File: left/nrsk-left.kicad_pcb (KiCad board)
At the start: 2 copper layers, 172.6 x 132.6 mm, 139 parts, among them J1 PJ-320D, J2 USB-C, J3 OLED 128x32, SW1 Esc, SW10 1, SW11 2, SW12 3, SW13 4, SW14 5, SW15 6, SW16 16, SW17 Tab, SW18 Q, SW19 W, SW2 F1, SW20 E, SW21 R, SW22 T, SW23 23, SW24 Ctrl, SW25 A, SW26 S, SW27 D, SW28 F, SW29 G, SW3 F2, SW30 30, SW31 Shift, SW32 Z, SW33 X, SW34 C, SW35 V, SW36 B, SW37 37, SW38 Ctrl, SW39 Opt, SW4 F3, SW40 Cmd, SW41 Space, SW42 Space, SW43 Space, SW44 44, SW5 F4, SW6 F5, SW7 F6, SW8 8, SW9 `, U1 RP2040, U2 USBLC6-2SC6, U3 AS5600-ASOM, U4 AP2112K-3.3, U5 W25Q128JVS, Y1 12MHz

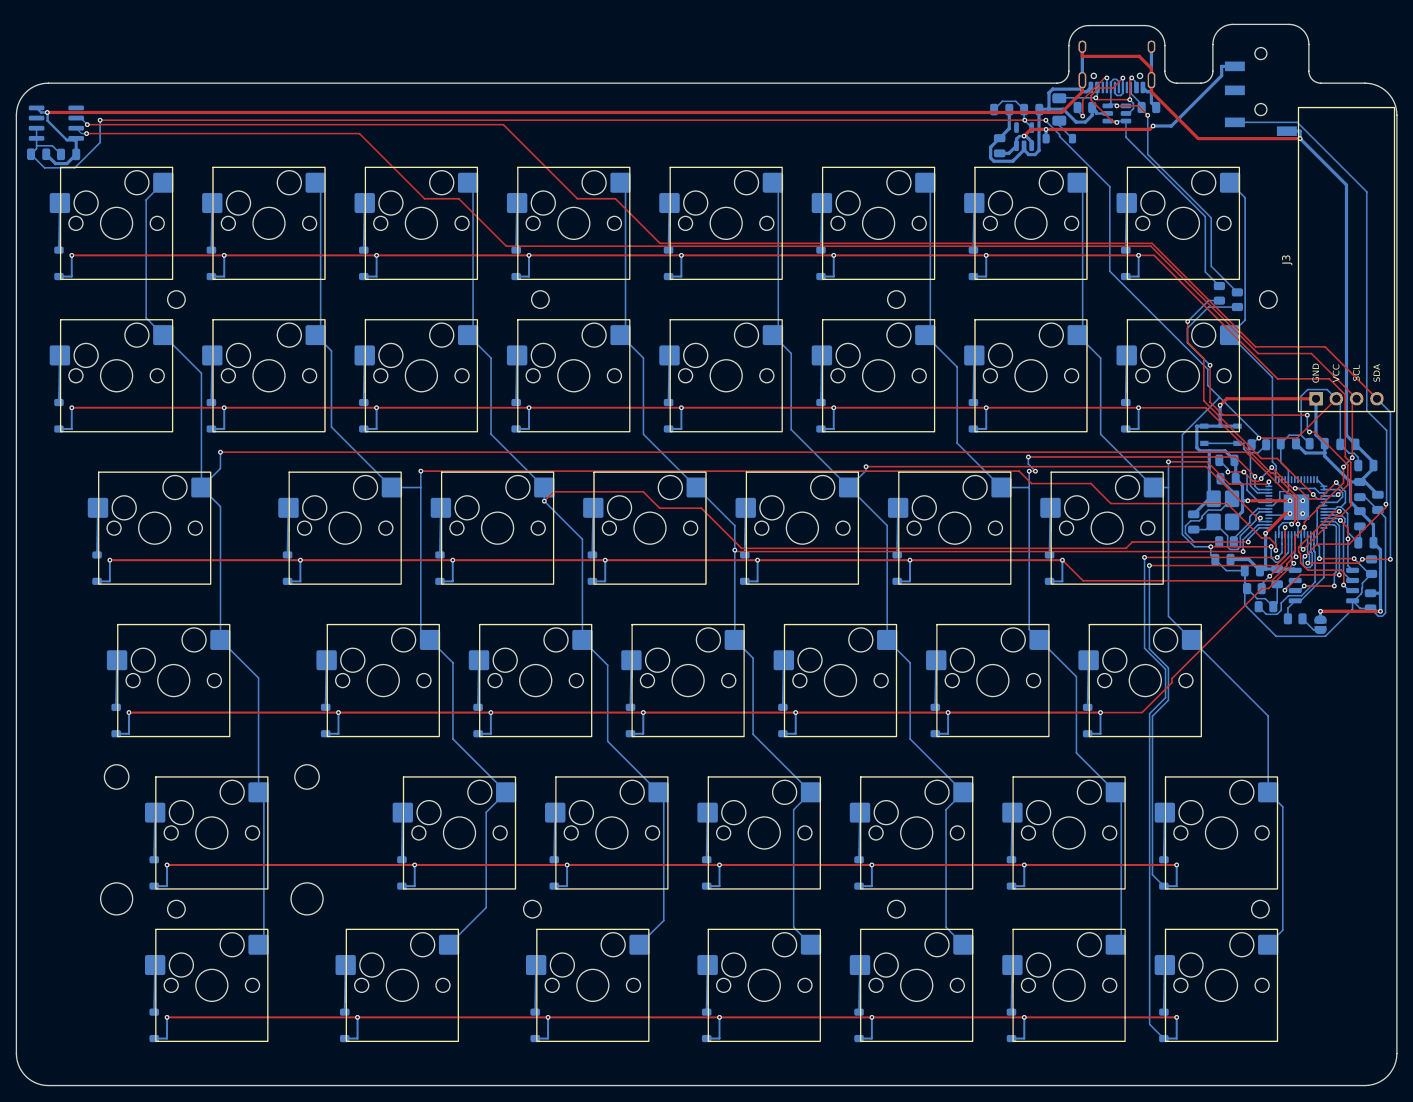
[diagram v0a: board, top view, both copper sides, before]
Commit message: PCB: thumbwheel encoder on the back at the wheel axis, boards re-routed (spec step 3) - ENC1 on the back, rotor on the wheel axis (where U3 was), terminals toward the board inside;   C9 / C10 gone from the support parts - The key turned 180 deg (socket below the stem) is now picked by geometry: a key whose   socket courtyard comes within 0.5 mm of the encoder courtyard. Left: Esc (SW1); right: none - Footprint Datasheet field left empty like the others (it differed from the symbol's) - Re-routed both halves; fab outputs regenerated - Checked: 0 unconnected, 0 DRC errors, 0 footprint errors, 0 schematic parity issues on   both halves (warnings: 5 silk-to-edge on J1/J2 as before, 3 / 2 dangling GND vias);   the gerber Edge.Cuts carries the rotor cut-out (3.1 mm square, lobes to +/-2.3 mm) at both wheel axes
Co-Authored-By: Claude Opus 5.5 <noreply@anthropic.com>
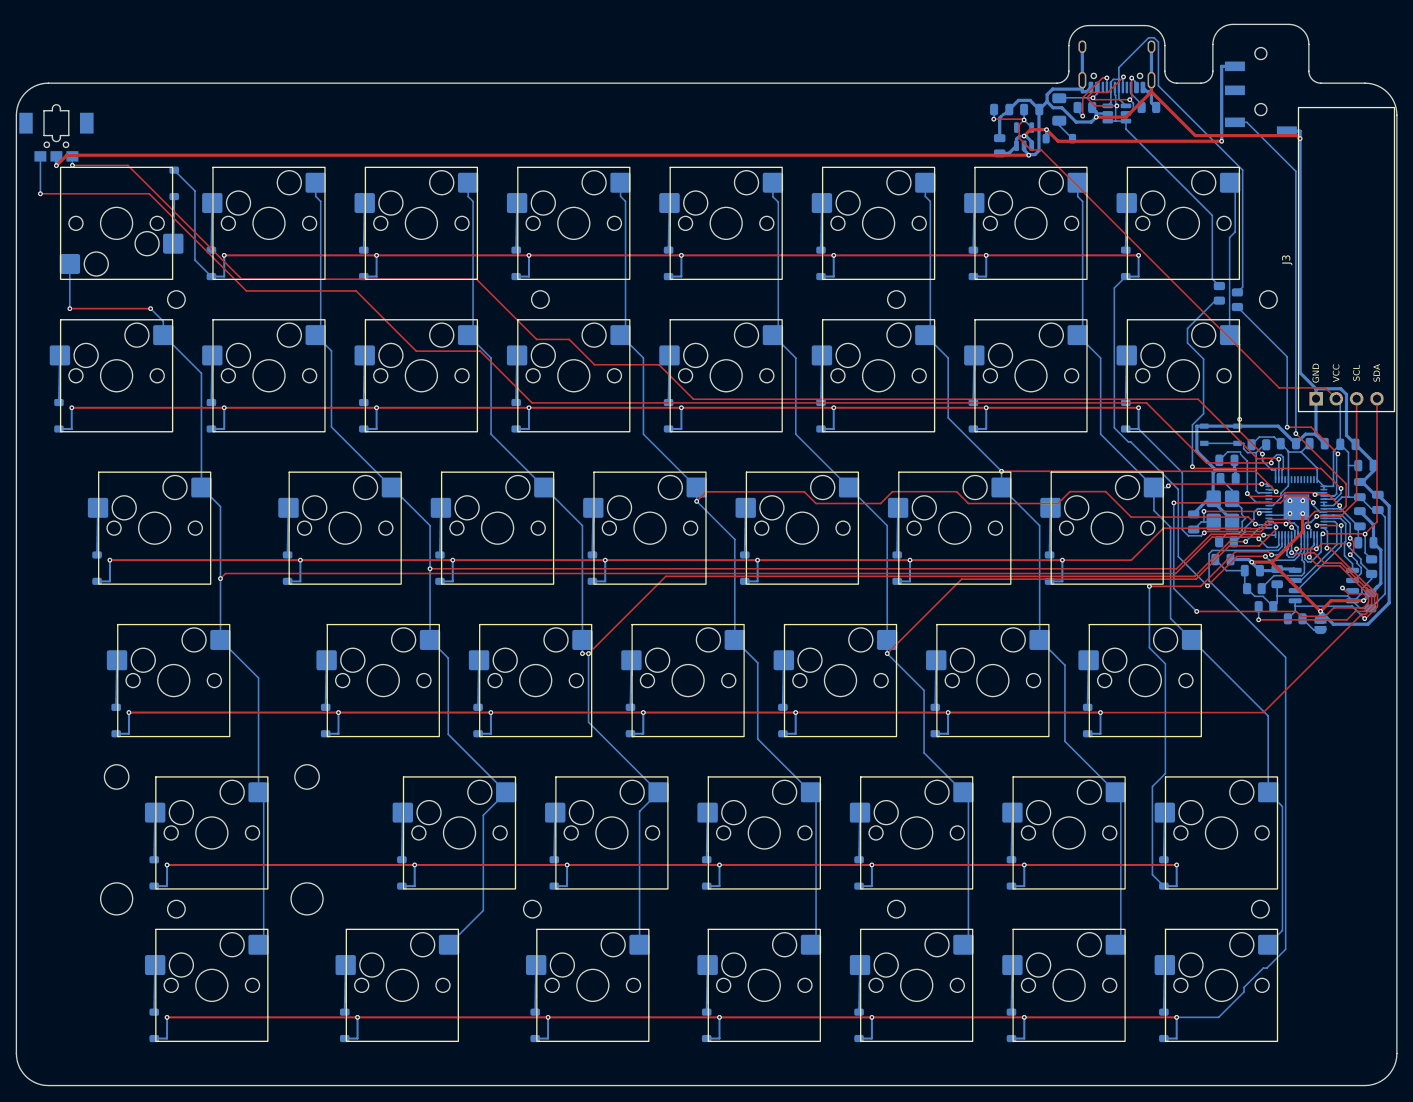
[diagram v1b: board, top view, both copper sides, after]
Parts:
- removed C10: 0.1uF, Capacitor_SMD:C_0805_2012Metric
- removed C9: 1uF, Capacitor_SMD:C_0805_2012Metric
- removed U3: AS5600-ASOM, Package_SO:SOIC-8_3.9x4.9mm_P1.27mm
- added ENC1: EC05E1220401, nrsk:Alps_EC05E1220401, B.Cu at (32.0, 27.0)
- moved D1 17.5 mm to (46.7, 34.5), turned to -90 degrees
- turned SW1 to 180 degrees
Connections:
- U1 pad 30: unconnected-(U1-GPIO19-Pad30) -> /ENC_A
- U1 pad 31: unconnected-(U1-GPIO20-Pad31) -> /ENC_B
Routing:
- net /3V3: track 367.1 -> 177.7 mm, vias 8 -> 5
- net /SDA: track 213.3 -> 34.5 mm, vias 4 -> 2
- net /ENC_B: track 0.00 -> 177.6 mm, vias 0 -> 2
- net /SCL: track 203.6 -> 33.0 mm, vias 5 -> 1
- net /ENC_A: track 0.00 -> 169.7 mm, vias 0 -> 2
- net /QSPI_SD3: track 19.8 -> 63.0 mm, vias 2 -> 4
- net GND: track 407.9 -> 385.7 mm
- net /ROW3: track 187.1 -> 207.2 mm
- net /DATA: track 79.7 -> 62.2 mm
- net /HAND: track 15.6 -> 30.4 mm, vias 0 -> 2
- net /USB_D-: track 38.3 -> 52.1 mm, vias 2 -> 0
- net /QSPI_SS: track 13.6 -> 27.2 mm, vias 0 -> 2
- net /D-: track 45.4 -> 32.1 mm, vias 4 -> 2
- net /COL0: track 250.8 -> 237.7 mm, vias 2 -> 4
- net /D+: track 35.9 -> 46.9 mm
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
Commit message: Board top edge +1 mm so the left Esc switch is no longer turned 180 deg
- TOP = MARGIN + 6.0 (was + 5.0), both halves, so they stay the same height. The wheel is
  placed from the corner, so it and its encoder move up 1 mm with the edge
- The Esc socket overlapped the encoder keep-out by 0.43 mm; it now clears it by 0.575 mm
  (1.075 mm between courtyards), so on_encoder() finds no key and every switch faces north.
  Checked on the generated boards: 0 of 44 / 48 switch footprints rotated (was 1 on the left)
- Board 172.6 / 199.6 x 126.3 mm, case 189.6 / 216.6 x 143.3 mm (each 1 mm taller)
- ./build.sh rerun: boards rerouted (0 unconnected), DRC 8 per side (5 silk at the connector
  mouths, 3 GND thermal vias), the same kinds as before; case checks pass; case, laser files,
  BOM, JLC files, assembly guide, 3D viewer and doc images regenerated. The left side was
  routed again once to drop a 1.2 mm dangling stub on D-
- README: sizes, the Esc note (all switches now face the same way); spec: note on the outcome
- Not rerun: the Blender renders (render_all.sh); they differ only by the 1 mm

Co-Authored-By: Claude Opus 5.5 <noreply@anthropic.com>
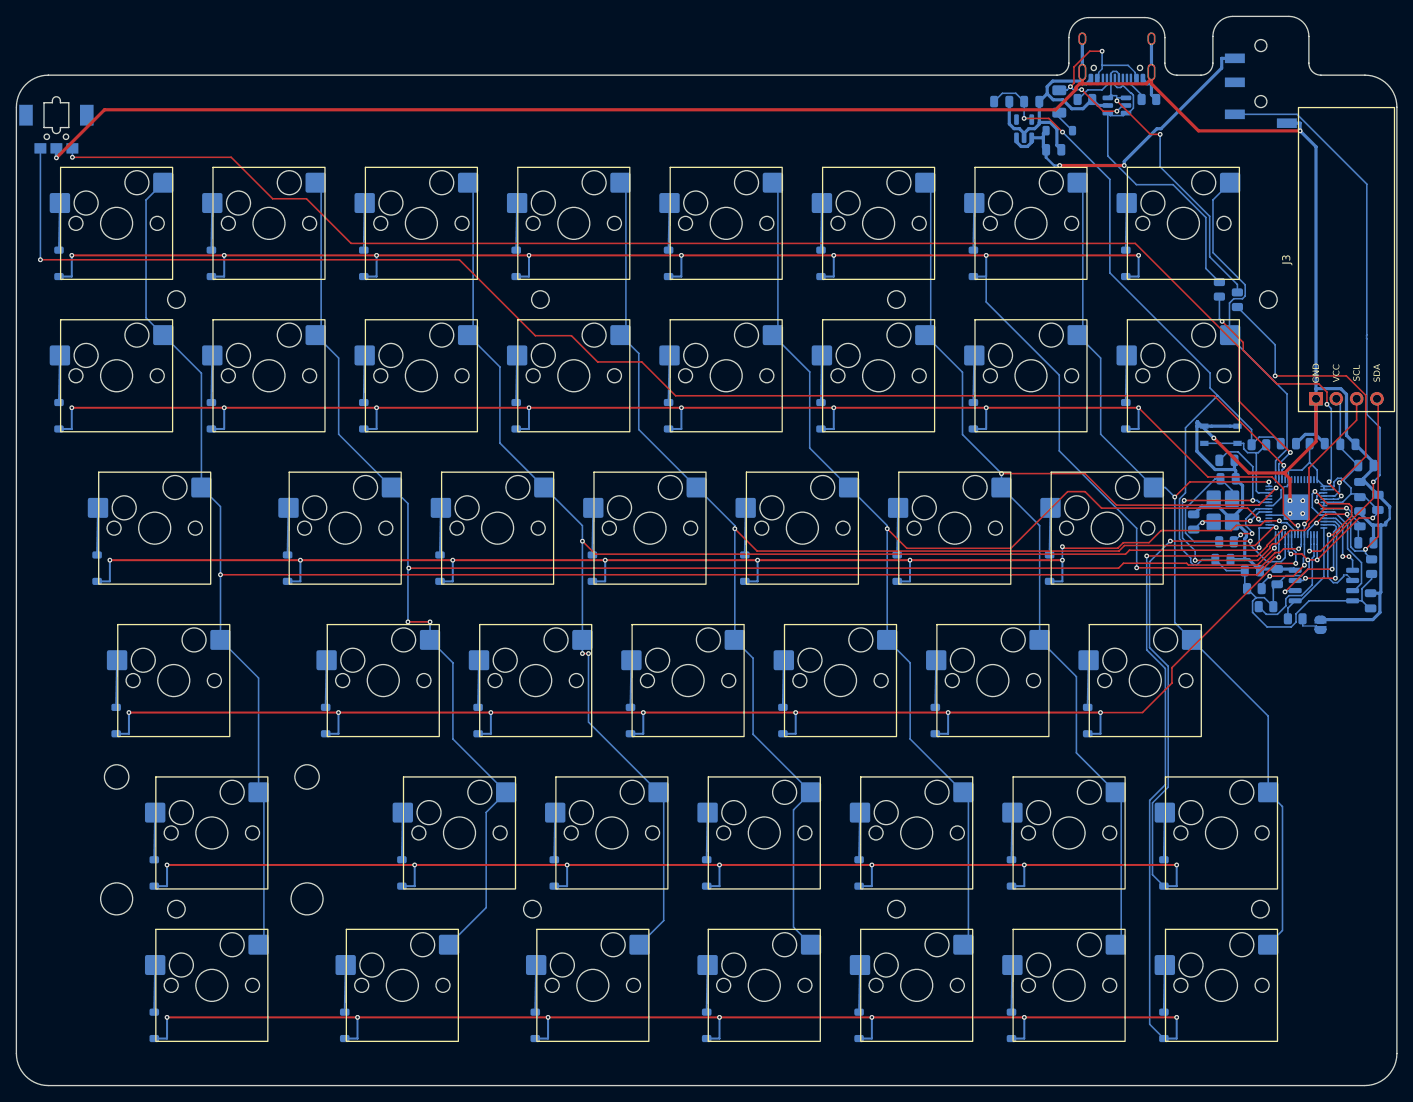
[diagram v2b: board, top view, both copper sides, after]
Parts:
- moved D1 17.5 mm to (32.3, 44.5), turned to 90 degrees
- moved C16 6.77 mm to (156.7, 30.3), turned to 0 degrees
- moved C17 1.00 mm to (153.9, 24.3)
- moved C19 1.00 mm to (150.2, 24.3)
- moved D99 1.00 mm to (157.4, 27.9)
- moved ENC1 1.00 mm to (32.0, 26.0)
- moved F1 1.00 mm to (157.4, 24.3)
- moved J1 1.00 mm to (182.6, 22.1)
- moved J2 1.00 mm to (164.6, 17.5)
- moved R4 1.00 mm to (160.6, 24.0)
- moved R5 1.00 mm to (168.6, 24.0)
- moved U2 1.00 mm to (164.6, 24.8)
- moved U4 1.00 mm to (153.0, 27.7)
- moved R2 0.50 mm to (177.4, 47.8)
- turned SW1 to 0 degrees
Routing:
- net /QSPI_SD3: track 63.0 -> 13.1 mm, vias 4 -> 0
- net /1V1: track 33.4 -> 61.5 mm, vias 3 -> 5
- net /3V3: track 177.7 -> 199.6 mm, vias 5 -> 6
- net /ROW3: track 207.2 -> 188.3 mm
- net /ROW0: track 219.7 -> 234.7 mm, vias 9 -> 10
- net /HAND: track 30.4 -> 15.5 mm, vias 2 -> 0
- net /QSPI_SS: track 27.2 -> 13.6 mm, vias 2 -> 0
- net /USB_D-: track 52.1 -> 38.7 mm, vias 0 -> 2
- net /QSPI_SCLK: track 12.3 -> 23.9 mm
- net /DATA: track 62.2 -> 73.3 mm
- net /D+: track 46.9 -> 36.9 mm, vias 2 -> 4
- net /VBUS: track 17.2 -> 26.3 mm, vias 3 -> 4
- net /ENC_A: track 169.7 -> 176.6 mm
- net /D-: track 32.1 -> 38.4 mm
- net GND: track 385.7 -> 391.4 mm, vias 11 -> 7
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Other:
- board size 172.6 x 132.6 mm -> 172.6 x 133.6 mm

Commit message: Right OLED turned like the left (header down); OLED pins fixed in the README
- The right OLED sat at 270 deg and the left at 90 deg, while the firmware uses one rotation
  (OLED_ROTATION_270) for both: one of the two displays would have been upside down. The right
  is now 90 deg too (header at the bottom); the module centre, and so the cover and the case,
  stay where they were
- case_data.json carries the OLED rotation; render_blender.py draws the glass from it instead of
  assuming the header end by side
- The MCU parts stay where they were placed by their pins. Mirroring the left cluster onto the
  right was tried: the right sockets are not mirrored and one (SW16) takes the room of the
  crystal group, and the RP2040 can only be turned, not mirrored, so the mirrored flash ended up
  at the far end of the QSPI pin row and the right board would not route (5-6 nets open, 3 tries)
- Boards: left routed again (placement unchanged), right re-placed and routed; both 0 unconnected,
  DRC 8 each (5 silk at the connector mouths, 3 GND thermal vias), 0 parity issues, ERC 0.
  Case, laser files, 3D viewer, assembly guide, BOM, JLC files and doc images regenerated
- JLC CPL checked pad by pad: each LCSC part's EasyEDA footprint placed as the CPL says lands on
  the same-numbered KiCad pads within 0.2 mm (21 part types, both halves; reset switch, TRRS and
  USB-C checked by position)
- Renders: render_all.sh (1600 px, 160 samples) and render_compare.sh
- README: OLED on GP3 (SCL) / GP2 (SDA) (it still said PD0 / PD1 from the Pro Micro days); both
  modules face the same way. docs/thumbwheel-check.md: check the text orientation, and how to
  flip it in make_qmk.py if it is upside down

Co-Authored-By: Claude Opus 5.5 <noreply@anthropic.com>
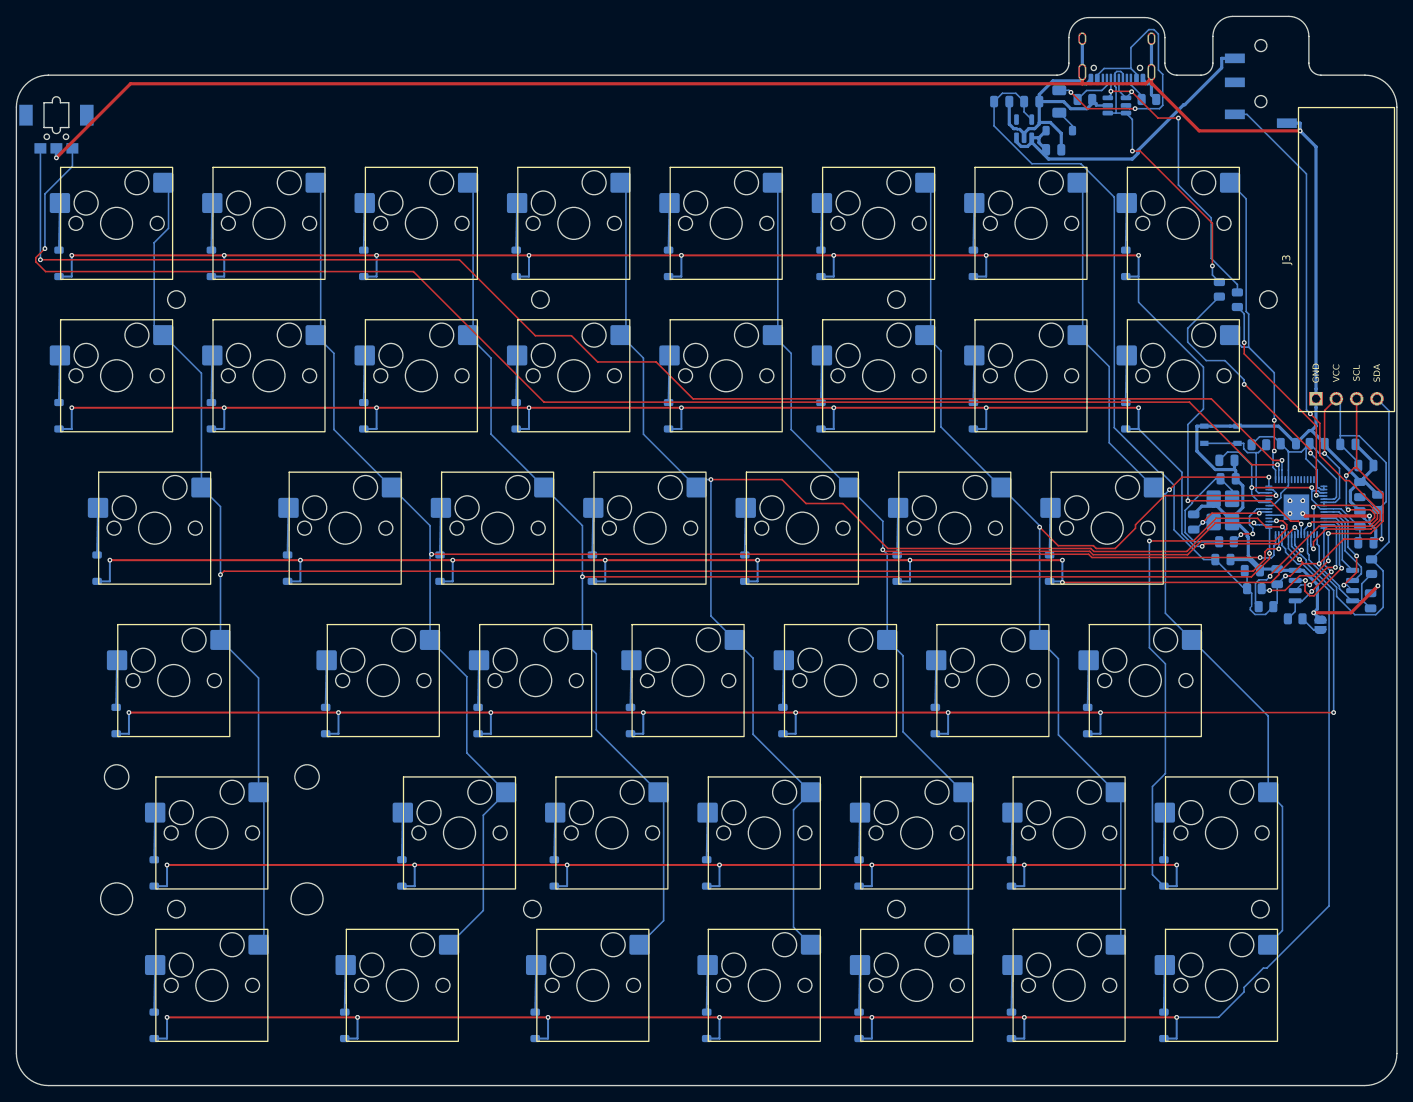
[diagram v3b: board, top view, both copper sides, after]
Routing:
- net /1V1: track 61.5 -> 31.6 mm, vias 5 -> 2
- net /SCL: track 30.5 -> 57.6 mm, vias 3 -> 6
- net /HAND: track 15.5 -> 34.5 mm, vias 0 -> 2
- net /ROW0: track 234.7 -> 216.2 mm
- net /ROW3: track 188.3 -> 204.8 mm
- net GND: track 391.4 -> 377.2 mm, vias 7 -> 9
- net /QSPI_SCLK: track 23.9 -> 11.7 mm, vias 2 -> 0
- net /VBUS: track 26.3 -> 38.5 mm, vias 4 -> 2
- net /SDA: track 33.8 -> 44.6 mm, vias 3 -> 0
- net /D-: track 38.4 -> 28.6 mm
- net /ROW5: track 238.6 -> 230.3 mm, vias 9 -> 7
- net /3V3: track 199.6 -> 207.2 mm, vias 6 -> 5
- net /ENC_A: track 176.6 -> 183.7 mm
- net /COL3: track 178.6 -> 185.0 mm
- net /COL1: track 221.5 -> 217.1 mm, vias 4 -> 2
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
